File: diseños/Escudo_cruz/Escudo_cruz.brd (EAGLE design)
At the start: 100 x 80 mm, 7 parts, among them J1 1X2-3.5MM, X1 TERMINAL-BLOCK-3.5MM-4-PIN-RO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

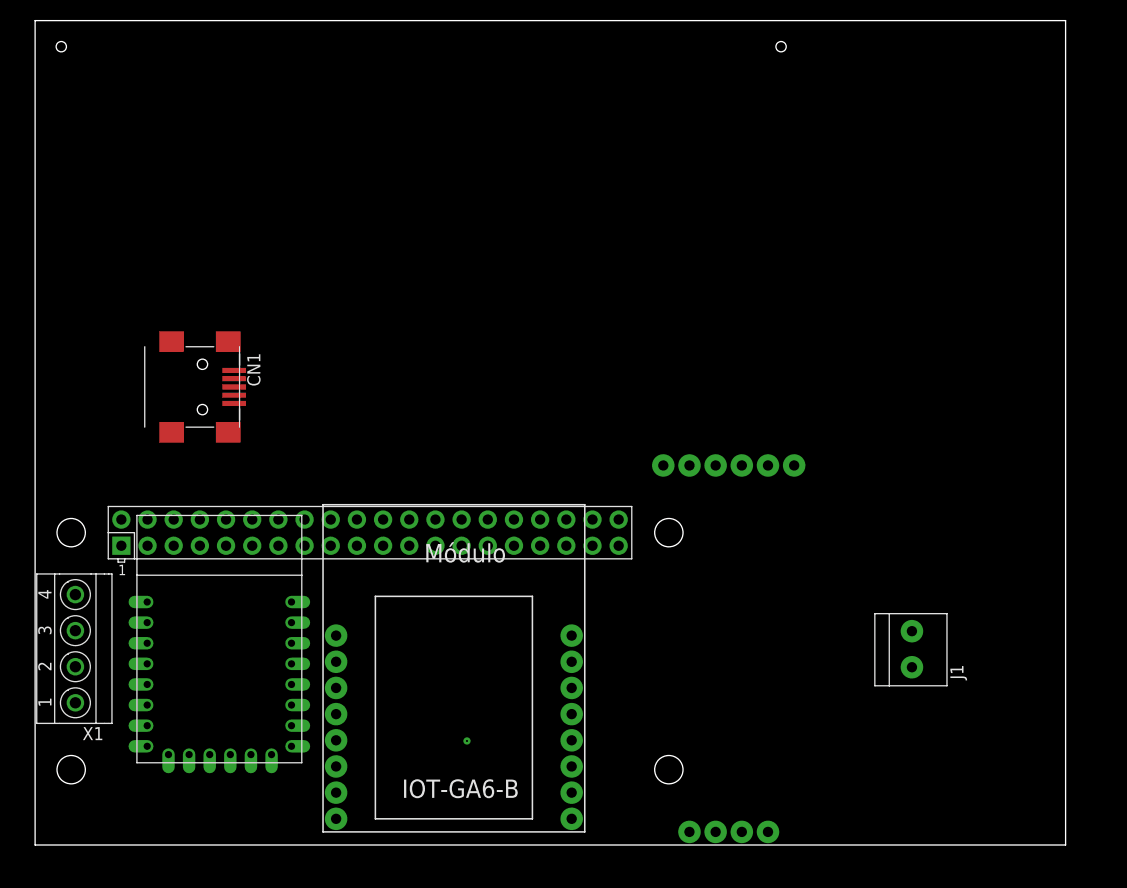
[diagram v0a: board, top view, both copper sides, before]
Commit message: Se agrega ESP para comunicarse mediante I2C con Raspberry
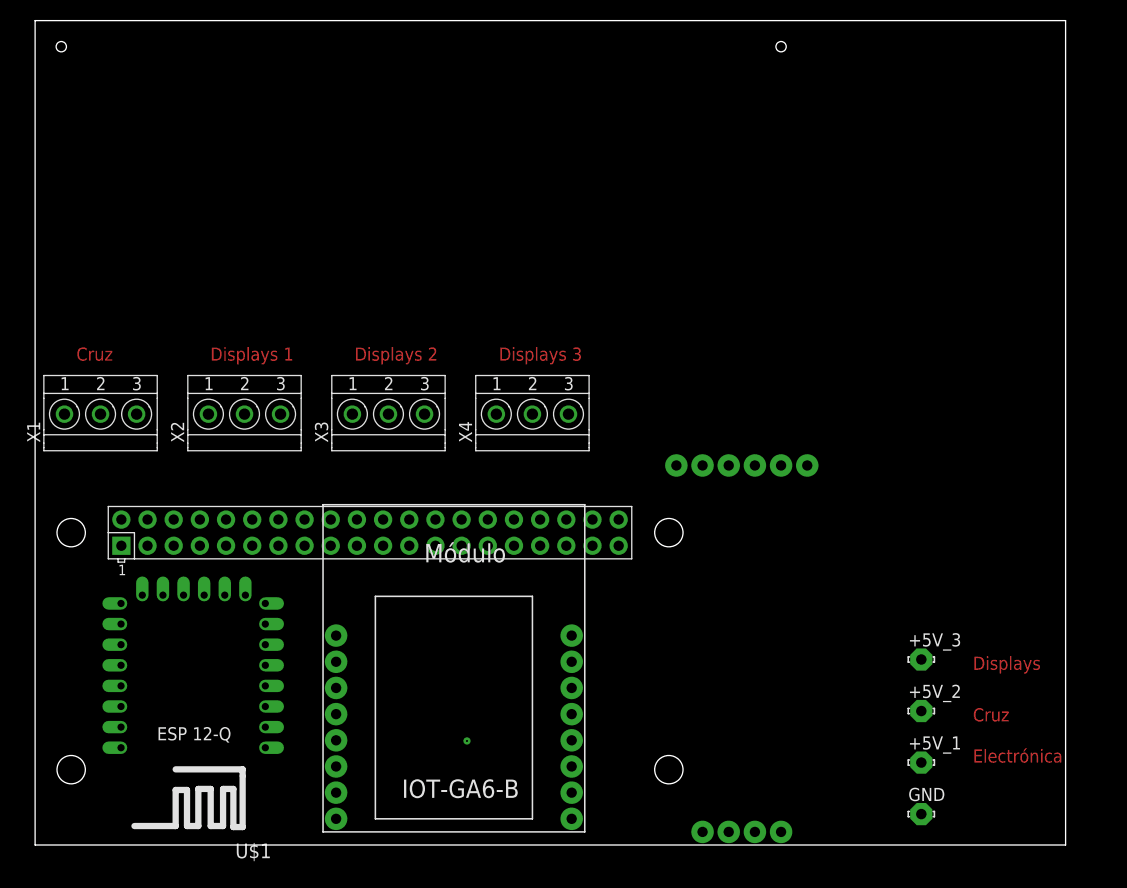
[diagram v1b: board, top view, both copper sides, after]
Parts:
- removed CN1: (no value), adafruit:USB-MINIB
- removed J1: 1X2-3.5MM, adafruit:1X2-3.5MM
- added +5V_1, +5V_2, +5V_3, GND: LSP10, solpad:LSP10
- added X2, X3, X4: TERMINAL-BLOCK-3.5MM-3-PIN-ROUND-PAD, Rembrandt Electronics - Terminal Block 3-5mm v1-0:TERMINAL-BLOCK-3-PIN-3.5MM-ROUND-PAD
- X1: value TERMINAL-BLOCK-3.5MM-4-PIN-ROUND-PAD -> TERMINAL-BLOCK-3.5MM-3-PIN-ROUND-PAD; device Rembrandt Electronics - Terminal Block 3-5mm v1-0:TERMINAL-BLOCK-4-PIN-3.5MM-ROUND-PAD -> Rembrandt Electronics - Terminal Block 3-5mm v1-0:TERMINAL-BLOCK-3-PIN-3.5MM-ROUND-PAD
- moved X1 23.0 mm to (6.35, 41.9), turned to 0 degrees
- moved U$1 3.59 mm to (15.2, 15.2), flipped to the top, turned to 180 degrees
- moved U$4 1.27 mm to (68.6, 38.1)
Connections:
- removed net 3V3@1: U$1.VCC, U$2.1
- removed net GND@3: J1.1, U$2.39, U$3.GND, U$4.GND
- removed net N$1 (its old number): J1.2, U$3.VCC, U$4.VCC
- removed net N$10: CN1.D-, U$1.TX
- removed net N$11: CN1.D+, U$1.RX
- removed net N$7 (its old number): U$1.GPIO4, X1.2
- removed net N$8: U$1.GPIO0, X1.3
- removed net N$9: U$1.GPIO2, X1.4
- removed net VBUS: CN1.VBUS
- new net +5V_1: +5V_1.MP, U$1.VCC, U$2.2, U$3.VCC, U$4.VCC
- new net +5V_2: +5V_2.MP, X1.2
- new net +5V_3: +5V_3.MP, X2.2, X3.2, X4.2
- new net GND: GND.MP, U$1.GND, U$3.GND, U$4.GND, X1.3, X2.3, X3.3, X4.3
- new net N$12: U$1.GPIO4, X2.1
- new net N$13: U$1.GPIO0, X3.1
- new net N$14: U$1.GPIO2, X4.1
- net GND@1: no longer CN1.GND, U$1.GND
- net N$3: now also U$1.GPIO12
- net N$4: now also U$1.GPIO14
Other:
- board text added: "Cruz"
- board text added: "Displays"
- board text added: "Displays 1"
- board text added: "Displays 2"
- board text added: "Displays 3"
- board text added: "Electrónica"
